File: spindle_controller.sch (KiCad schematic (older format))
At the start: 60 parts, among them J1 VAC 230V, J2 AUX/CONTROL, J3 ICP, J4 Load output, J5 CONN_01X03, J6 CONN_01X03, Q1 2N3904, SW1 Rotary_Encoder_Switch, T1 230 - 6VAC (Spitznagel SPK 01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, U1 LM7805CT, U2 ATMEGA328P-PU, U3 PC817, U4 MOC3020M, U5 TCRT5000, U6 AP111750, Y1 16MHz

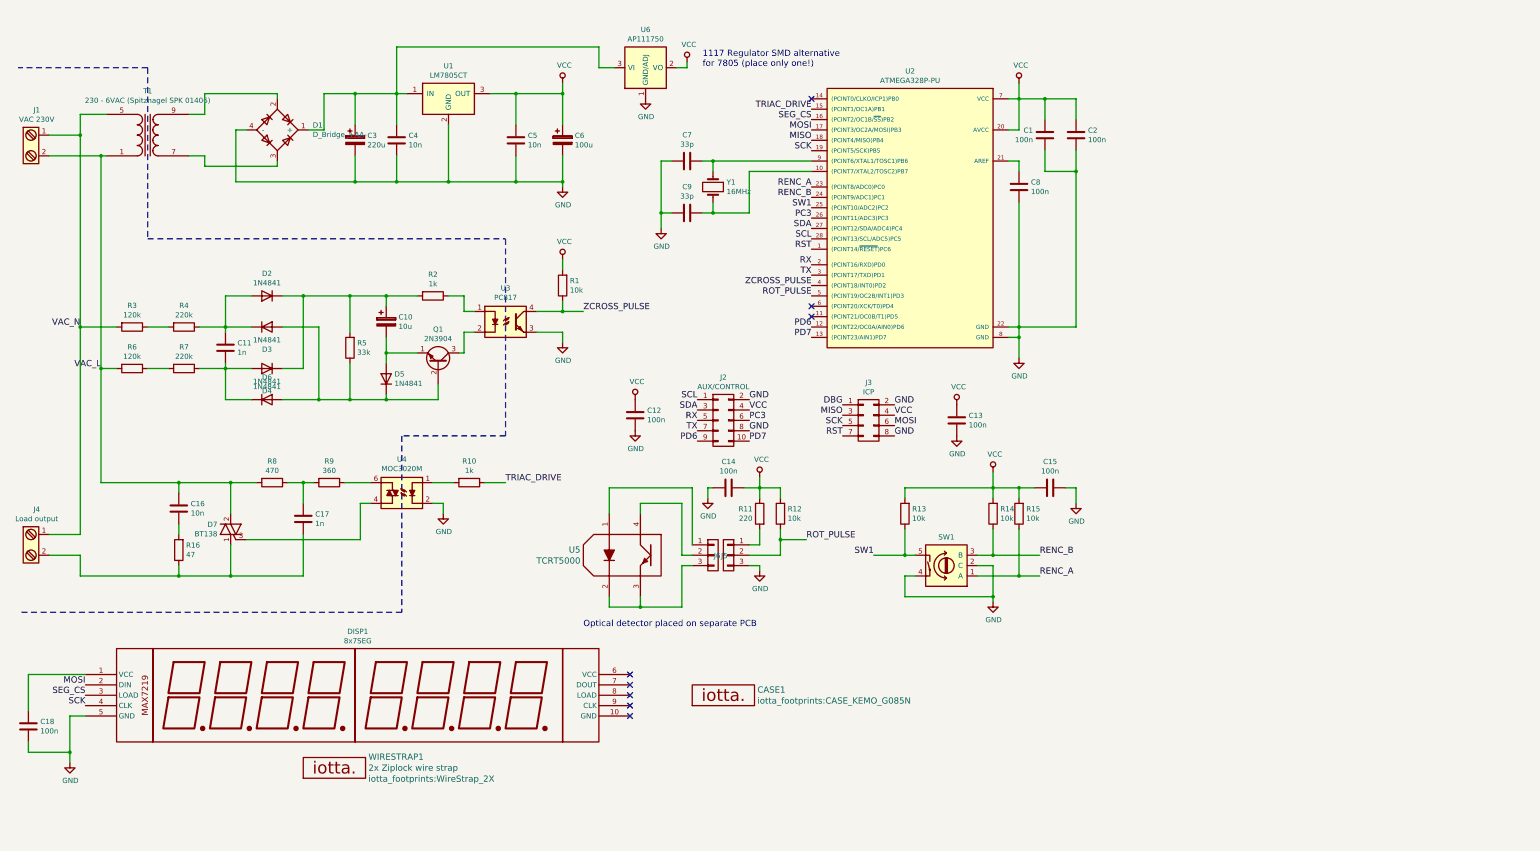
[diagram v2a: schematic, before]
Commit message: Finish routing. Need to draw break-off slots.
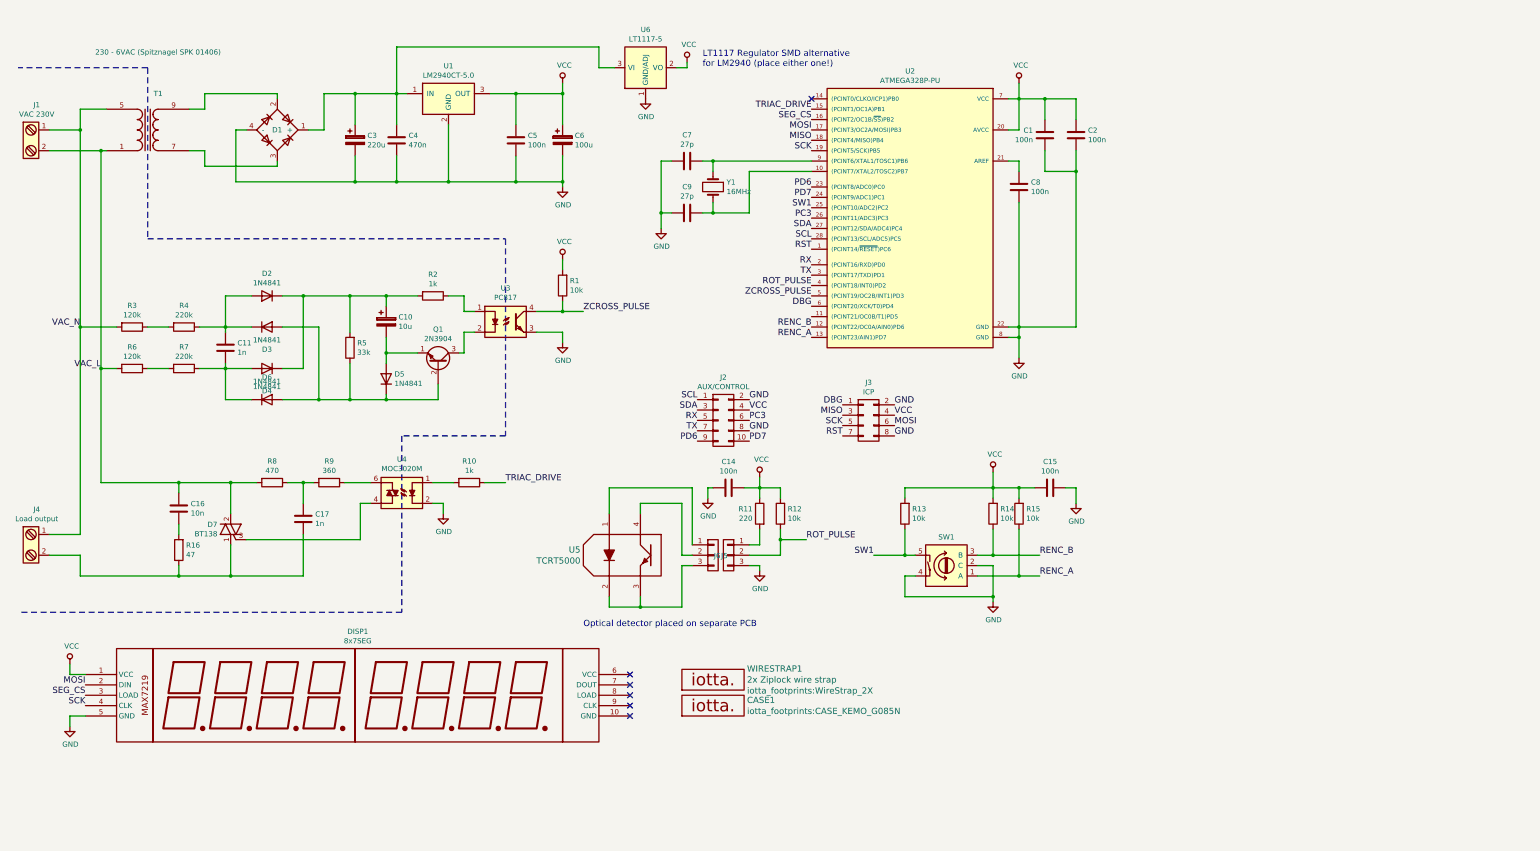
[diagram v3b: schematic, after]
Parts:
- removed C12, C13, C18: 100n, Capacitors_ThroughHole:C_Rect_L7.0mm_W2.5mm_P5.00mm, symbol C
- C4: value 10n -> 470n
- C5: value 10n -> 100n
- C7, C9: value 33p -> 27p
- J2: footprint Pin_Headers:Pin_Header_Straight_2x05_Pitch2.54mm -> Pin_Headers:Pin_Header_Angled_2x05_Pitch2.54mm
- J3: footprint Pin_Headers:Pin_Header_Straight_2x04_Pitch2.54mm -> Pin_Headers:Pin_Header_Angled_2x04_Pitch2.54mm
- J5, J6: footprint Pin_Headers:Pin_Header_Straight_1x03_Pitch2.54mm -> Pin_Headers:Pin_Header_Angled_1x03_Pitch2.54mm
- U1: value LM7805CT -> LM2940CT-5.0
- U6: value AP111750 -> LT1117-5
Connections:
- net DBG: now also U2.6 ((PCINT20/XCK/T0)PD4)
- net PD6: now also U2.23 ((PCINT8/ADC0)PC0); no longer U2.12 ((PCINT22/OC0A/AIN0)PD6)
- net PD7: now also U2.24 ((PCINT9/ADC1)PC1); no longer U2.13 ((PCINT23/AIN1)PD7)
- net RENC_A: now also U2.13 ((PCINT23/AIN1)PD7); no longer U2.23 ((PCINT8/ADC0)PC0)
- net RENC_B: now also U2.12 ((PCINT22/OC0A/AIN0)PD6); no longer U2.24 ((PCINT9/ADC1)PC1)
- net ROT_PULSE: now also U2.4 ((PCINT18/INT0)PD2); no longer U2.5 ((PCINT19/OC2B/INT1)PD3)
- net VCC: now also DISP1.1 (VCC)
- net ZCROSS_PULSE: now also U2.5 ((PCINT19/OC2B/INT1)PD3); no longer U2.4 ((PCINT18/INT0)PD2)
- no-connect marks 8 -> 6
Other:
- note added: "LT1117 Regulator SMD alternative\nfor LM2940 (place either one!)"
- note removed: "1117 Regulator SMD alternative\nfor 7805 (place only one!)"
- moved on the sheet: CASE1, J1, T1, WIRESTRAP1

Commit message: Add jumper wires for single sided PCB's
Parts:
- added J7: GND_JUMPER, iotta_footprints:JUMPER_PIN, symbol CONN_01X01
- added J8: VCC_JUMPER, iotta_footprints:JUMPER_PIN, symbol CONN_01X01
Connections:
- net GND: now also J7.1 (P1)
- net VCC: now also J8.1 (P1)
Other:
- note added: "Jumper ends for\nsingle sided board"
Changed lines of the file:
@@
 Wire Wire Line
 	1150 6650 1300 6650
+$Comp
+L CONN_01X01 J8
+U 1 1 58F34CD2
+P 5250 5850
+F 0 "J8" V 5122 5928 50  0000 L CNN
+F 1 "VCC_JUMPER" V 5200 5950 50  0001 L CNN
+F 2 "iotta_footprints:JUMPER_PIN" H -450 300 50  0001 C CNN
+F 3 "" H -450 300 50  0001 C CNN
+	1    5250 5850
+	0    1    1    0
+$EndComp
+$Comp
+L CONN_01X01 J7
+U 1 1 58F35044
+P 4950 5600
+F 0 "J7" V 4915 5512 50  0000 R CNN
+F 1 "GND_JUMPER" V 4800 5500 50  0001 R CNN
+F 2 "iotta_footprints:JUMPER_PIN" H -750 50  50  0001 C CNN
+F 3 "" H -750 50  50  0001 C CNN
+	1    4950 5600
+	0    -1   -1   0
+$EndComp
+$Comp
+L VCC #PWR019
+U 1 1 58F35416
+P 5250 5650
+F 0 "#PWR019" H 5250 5500 50  0001 C CNN
+F 1 "VCC" H 5267 5823 50  0000 C CNN
+F 2 "" H 5250 5650 50  0001 C CNN
+F 3 "" H 5250 5650 50  0001 C CNN
+	1    5250 5650
+	1    0    0    -1
+$EndComp
+$Comp
+L GND #PWR020
+U 1 1 58F35497
+P 4950 5800
+F 0 "#PWR020" H 4950 5550 50  0001 C CNN
+F 1 "GND" H 4955 5627 50  0000 C CNN
+F 2 "" H 4950 5800 50  0001 C CNN
+F 3 "" H 4950 5800 50  0001 C CNN
+	1    4950 5800
+	1    0    0    -1
+$EndComp
+Text Notes 4750 6250 0    60   ~ 0
+Jumper ends for\nsingle sided board
 $EndSCHEMATC

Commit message: Add breakaway board for optical sensor, general board updates, dissipation planes, screw clearances and silkscreen
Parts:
- CASE1: footprint iotta_footprints:CASE_KEMO_G085N -> iotta_footprints:CASE_KEMO_G085N+BREAKAWAY_SENSOR
- U2: renamed from U1; footprint TO_SOT_Packages_THT:TO-220_Horizontal -> iotta_footprints:TO-220_Horizontal_connected_tab
- WIRESTRAP1: footprint iotta_footprints:WireStrap_2X -> iotta_footprints:WireStrap_2X_5HOLES
- renumbered D1 to BR1, C14 to C12, C15 to C13, C16 to C14, C17 to C15, D2 to D1, D3 to D2, D4 to D3, D5 to D4, D6 to D5, D7 to TRIAC1, U6 to U1, U2 to U3, U3 to U4, U4 to U5, U5 to U6
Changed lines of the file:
@@
 $EndComp
 $Comp
-L ATMEGA328P-PU U2
+L ATMEGA328P-PU U3
 U 1 1 58F0A167
 P 9300 2200
-F 0 "U2" H 9350 3567 50  0000 C CNN
+F 0 "U3" H 9350 3567 50  0000 C CNN
 F 1 "ATMEGA328P-PU" H 9350 3476 50  0000 C CNN
 F 2 "Housings_DIP:DIP-28_W7.62mm" H 9300 2200 50  0001 C CIN
@@
 $EndComp
 $Comp
-L MOC3020M U4
+L MOC3020M U5
 U 1 1 58F0A616
 P 4350 4900
-F 0 "U4" H 4350 5225 50  0000 C CNN
+F 0 "U5" H 4350 5225 50  0000 C CNN
 F 1 "MOC3020M" H 4350 5134 50  0000 C CNN
 F 2 "Housings_DIP:DIP-6_W7.62mm" H 4150 4700 50  0001 L CIN
@@
 $EndComp
 $Comp
-L Q_TRIAC_A1A2G D7
+L Q_TRIAC_A1A2G TRIAC1
 U 1 1 58F0AE6B
 P 2700 5250
-F 0 "D7" H 2828 5296 50  0000 L CNN
+F 0 "TRIAC1" H 2828 5296 50  0000 L CNN
 F 1 "BT138" H 2828 5205 50  0000 L CNN
 F 2 "TO_SOT_Packages_THT:TO-220_Vertical" V 2775 5275 50  0001 C CNN
@@
 $EndComp
 $Comp
-L PC817 U3
+L PC817 U4
 U 1 1 58F0AFEA
 P 5350 3250
-F 0 "U3" H 5350 3575 50  0000 C CNN
+F 0 "U4" H 5350 3575 50  0000 C CNN
 F 1 "PC817" H 5350 3484 50  0000 C CNN
 F 2 "Housings_DIP:DIP-4_W7.62mm" H 5150 3050 50  0001 L CIN
@@
 $EndComp
 $Comp
-L D D3
+L D D2
 U 1 1 58F0B25B
 P 3050 3300
-F 0 "D3" H 3050 3084 50  0000 C CNN
+F 0 "D2" H 3050 3084 50  0000 C CNN
 F 1 "1N4841" H 3050 3175 50  0000 C CNN
 F 2 "w_pth_diodes:diode_do35" H 3050 3300 50  0001 C CNN
@@
 $EndComp
 $Comp
-L D D4
+L D D3
 U 1 1 58F0B327
 P 3050 3700
-F 0 "D4" H 3050 3916 50  0000 C CNN
+F 0 "D3" H 3050 3916 50  0000 C CNN
 F 1 "1N4841" H 3050 3825 50  0000 C CNN
 F 2 "w_pth_diodes:diode_do35" H 3050 3700 50  0001 C CNN
@@
 $EndComp
 $Comp
-L D D6
+L D D5
 U 1 1 58F0B35F
 P 3050 4000
-F 0 "D6" H 3050 4216 50  0000 C CNN
+F 0 "D5" H 3050 4216 50  0000 C CNN
 F 1 "1N4841" H 3050 4125 50  0000 C CNN
 F 2 "w_pth_diodes:diode_do35" H 3050 4000 50  0001 C CNN
@@
 $EndComp
 $Comp
-L D D2
+L D D1
 U 1 1 58F0B393
 P 3050 3000
-F 0 "D2" H 3050 2784 50  0000 C CNN
+F 0 "D1" H 3050 2784 50  0000 C CNN
 F 1 "1N4841" H 3050 2875 50  0000 C CNN
 F 2 "w_pth_diodes:diode_do35" H 3050 3000 50  0001 C CNN
@@
 $EndComp
 $Comp
-L D D5
+L D D4
 U 1 1 58F0C123
 P 4200 3800
-F 0 "D5" V 4246 3721 50  0000 R CNN
+F 0 "D4" V 4246 3721 50  0000 R CNN
 F 1 "1N4841" V 4155 3721 50  0000 R CNN
 F 2 "w_pth_diodes:diode_do35" H 4200 3800 50  0001 C CNN
@@
 $EndComp
 $Comp
-L C C17
+L C C15
 U 1 1 58F0D9A4
 P 3400 5150
-F 0 "C17" H 3515 5196 50  0000 L CNN
+F 0 "C15" H 3515 5196 50  0000 L CNN
 F 1 "1n" H 3515 5105 50  0000 L CNN
 F 2 "Capacitors_ThroughHole:C_Disc_D8.0mm_W5.0mm_P7.50mm" H 3438 5000 50  0001 C CNN
@@
 $EndComp
 $Comp
-L C C16
+L C C14
 U 1 1 58F0DA06
 P 2200 5050
-F 0 "C16" H 2315 5096 50  0000 L CNN
+F 0 "C14" H 2315 5096 50  0000 L CNN
 F 1 "10n" H 2315 5005 50  0000 L CNN
 F 2 "Capacitors_ThroughHole:C_Rect_L16.5mm_W5.0mm_P15.00mm_MKT" H 2238 4900 50  0001 C CNN
@@
 $EndComp
 $Comp
-L TCRT5000 U5
+L TCRT5000 U6
 U 1 1 58F1825E
 P 6500 5500
-F 0 "U5" H 6928 5553 60  0000 L CNN
+F 0 "U6" H 6928 5553 60  0000 L CNN
 F 1 "TCRT5000" H 6928 5447 60  0000 L CNN
 F 2 "iotta_footprints:TCRT5000" V 6600 5500 60  0001 C CNN
@@
 $EndComp
 $Comp
-L C C15
+L C C13
 U 1 1 58F1C311
 P 10600 4850
-F 0 "C15" V 10348 4850 50  0000 C CNN
+F 0 "C13" V 10348 4850 50  0000 C CNN
 F 1 "100n" V 10439 4850 50  0000 C CNN
 F 2 "Capacitors_ThroughHole:C_Rect_L7.0mm_W2.5mm_P5.00mm" H 10638 4700 50  0001 C CNN
@@
 $EndComp
 $Comp
-L C C14
+L C C12
 U 1 1 58F1C80E
 P 7500 4850
-F 0 "C14" V 7248 4850 50  0000 C CNN
+F 0 "C12" V 7248 4850 50  0000 C CNN
 F 1 "100n" V 7339 4850 50  0000 C CNN
 F 2 "Capacitors_ThroughHole:C_Rect_L7.0mm_W2.5mm_P5.00mm" H 7538 4700 50  0001 C CNN
@@
 	1900 800  650  800
 $Comp
-L D_Bridge_+AA- D1
+L D_Bridge_+AA- BR1
 U 1 1 58F0DEBA
 P 3150 1400
-F 0 "D1" H 3100 1400 50  0000 L CNN
+F 0 "BR1" H 3100 1400 50  0000 L CNN
 F 1 "D_Bridge_+AA-" H 3300 1100 50  0001 L CNN
 F 2 "w_pth_diodes:bridge_wob" H 3150 1400 50  0001 C CNN
@@
 $EndComp
 $Comp
-L LM7805CT U1
+L LM7805CT U2
 U 1 1 58F0F97F
 P 4800 1100
-F 0 "U1" H 4800 1417 50  0000 C CNN
+F 0 "U2" H 4800 1417 50  0000 C CNN
 F 1 "LM2940CT-5.0" H 4800 1326 50  0000 C CNN
-F 2 "TO_SOT_Packages_THT:TO-220_Horizontal" H 4800 1200 50  0001 C CIN
+F 2 "iotta_footprints:TO-220_Horizontal_connected_tab" H 4800 1200 50  0001 C CIN
 F 3 "" H 4800 1100 50  0001 C CNN
 	1    4800 1100
@@
 F 0 "CASE1" H 7678 7203 60  0000 L CNN
 F 1 "Case" H 7678 7150 60  0001 L CNN
-F 2 "iotta_footprints:CASE_KEMO_G085N" H 7678 7097 60  0000 L CNN
+F 2 "iotta_footprints:CASE_KEMO_G085N+BREAKAWAY_SENSOR" H 7678 7097 60  0000 L CNN
 F 3 "" H 7050 7050 60  0000 C CNN
 	1    7050 7050
@@
 $EndComp
 $Comp
-L AP111750 U6
+L AP111750 U1
 U 1 1 58F26D3E
 P 6700 800
-F 0 "U6" H 6700 1167 50  0000 C CNN
+F 0 "U1" H 6700 1167 50  0000 C CNN
 F 1 "LT1117-5" H 6700 1076 50  0000 C CNN
 F 2 "TO_SOT_Packages_SMD:SOT-223" H 6700 450 50  0001 C CNN
@@
 F 0 "WIRESTRAP1" H 7678 7006 60  0000 L CNN
 F 1 "2x Ziplock wire strap" H 7678 6900 60  0000 L CNN
-F 2 "iotta_footprints:WireStrap_2X" H 7678 6794 60  0000 L CNN
+F 2 "iotta_footprints:WireStrap_2X_5HOLES" H 7678 6794 60  0000 L CNN
 F 3 "" H 7050 6800 60  0000 C CNN
 	1    7050 6800

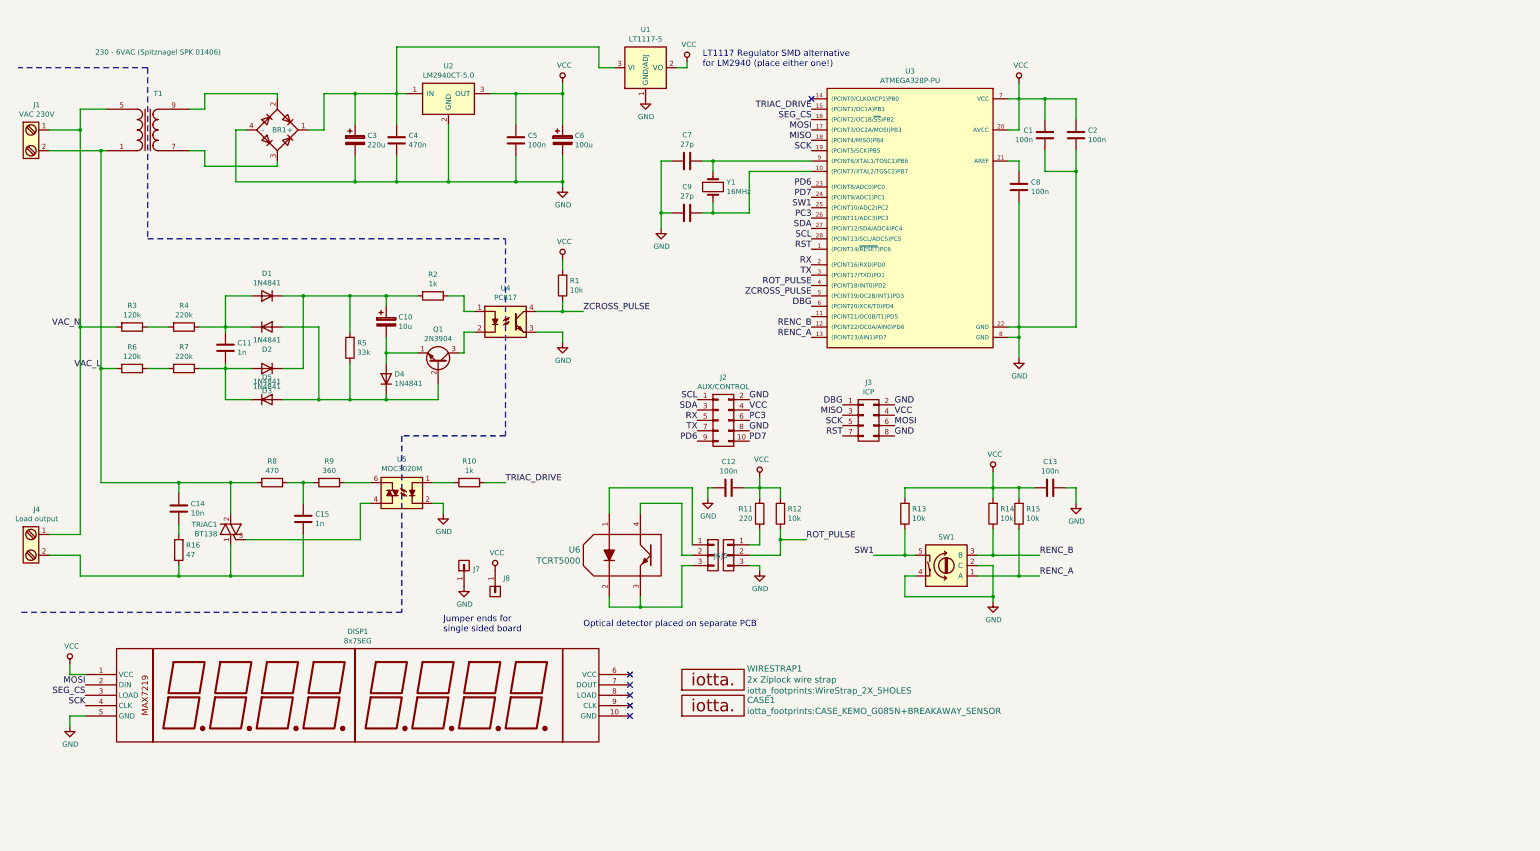
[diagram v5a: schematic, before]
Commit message: Rearranged pin ouputs (PB0 and PC3 now separate), added rotary debounce (not on PCB yet), added 3mm jack for optical pickup
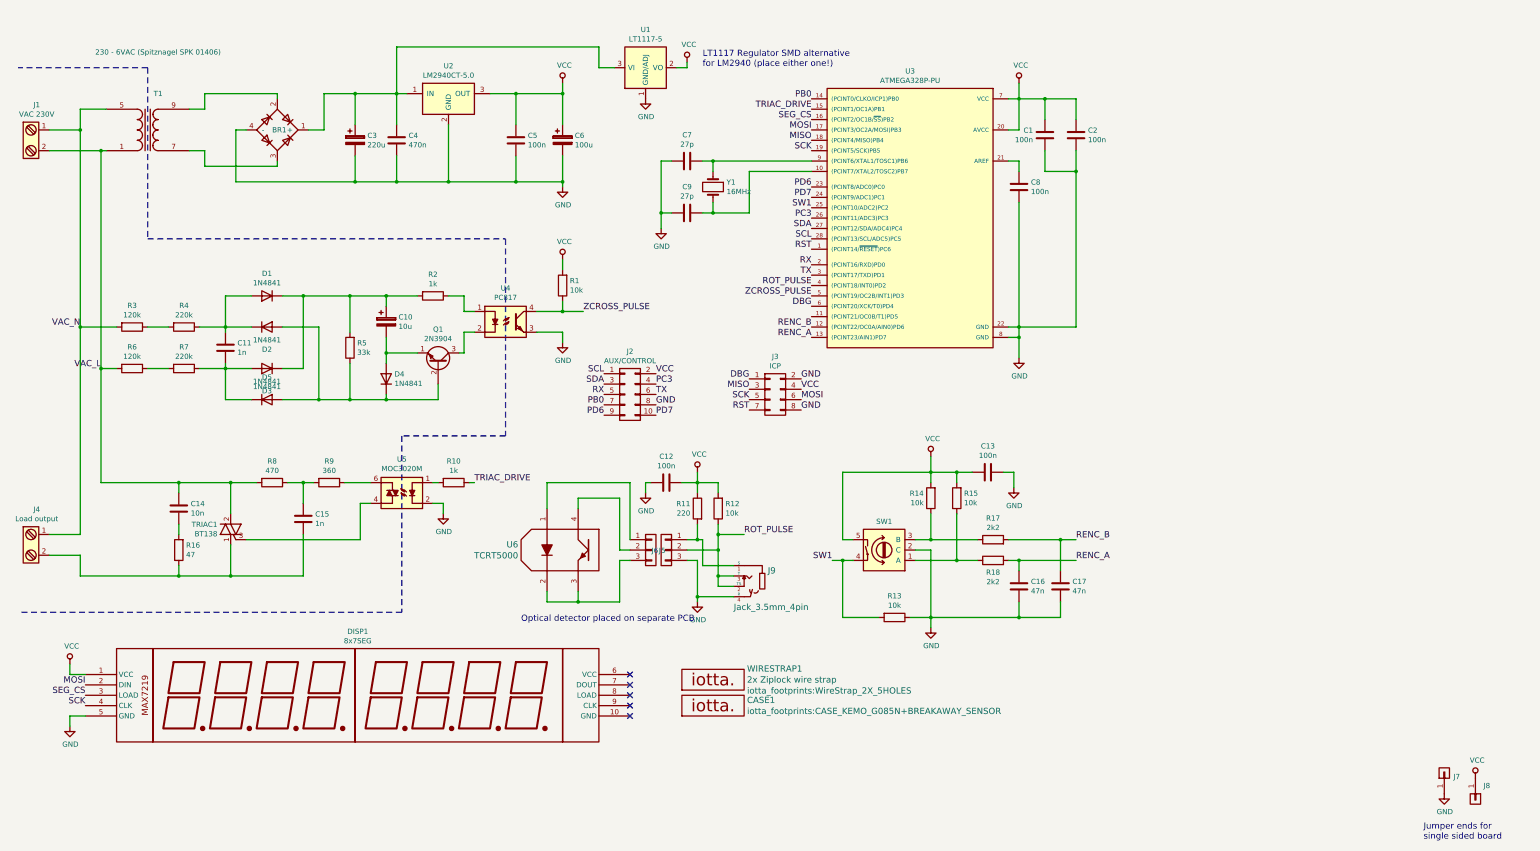
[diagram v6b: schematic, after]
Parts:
- added C16, C17: 47n, Capacitors_ThroughHole:C_Rect_L7.0mm_W2.5mm_P5.00mm, symbol C
- added J9: Jack_3.5mm_4pin, w_conn_av:jack_3.5_sj1-3514-smt, symbol Jack_3.5mm_4pin
- added R17, R18: 2k2, Resistors_ThroughHole:R_Axial_DIN0204_L3.6mm_D1.6mm_P7.62mm_Horizontal, symbol R
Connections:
- net GND: now also R13.1, C16.1, C17.1, J9.4 (R); no longer J2.2 (P2), SW1.4
- net PC3: now also J2.4 (P4); no longer J2.6 (P6)
- net RENC_A: now also C16.2, R18.2; no longer R15.1, SW1.1 (A)
- net RENC_B: now also C17.2, R17.2; no longer R14.1, SW1.3 (B)
- net ROT_PULSE: now also J9.2 (TS), J9.3 (T)
- net SW1: now also R13.2, SW1.4; no longer R13.1, SW1.5
- net TX: now also J2.6 (P6); no longer J2.7 (P7)
- net VCC: now also J2.2 (P2), SW1.5; no longer J2.4 (P4), R13.2
- net PB0: now reaches U3.14 ((PCINT0/CLKO/ICP1)PB0)
- net PB0: now also J2.7 (P7)
- net at J6.1 (P1), R11.2: now also J9.1 (S)
- new net: R15.1, R18.1, SW1.1 (A)
- new net: R14.1, R17.1, SW1.3 (B)
- no-connect marks 6 -> 5
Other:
- moved on the sheet: C12, C13, J2, J3, J5, J6, J7, J8, R10, R11, R12, R13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
